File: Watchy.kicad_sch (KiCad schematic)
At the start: 74 parts, among them J1 FPC24(0.5MM), J2 USB_C_Receptacle_USB2.0, J4 Conn_01x01, J5 Conn_01x01, M1 Vibration_Motor, Q1 AO3400A, Q2 UMH3N, Q4 CJ2301, Q5 S8050, SW1 BTN, SW2 BTN, SW3 BTN, SW4 BTN, U1 ESP32-PICO-D4, U2 ME6211C33M5G-N, U3 CP2102, U4 BMA423, U5 TP4054, U6 PCF8563BS, Y1 32.768KHz

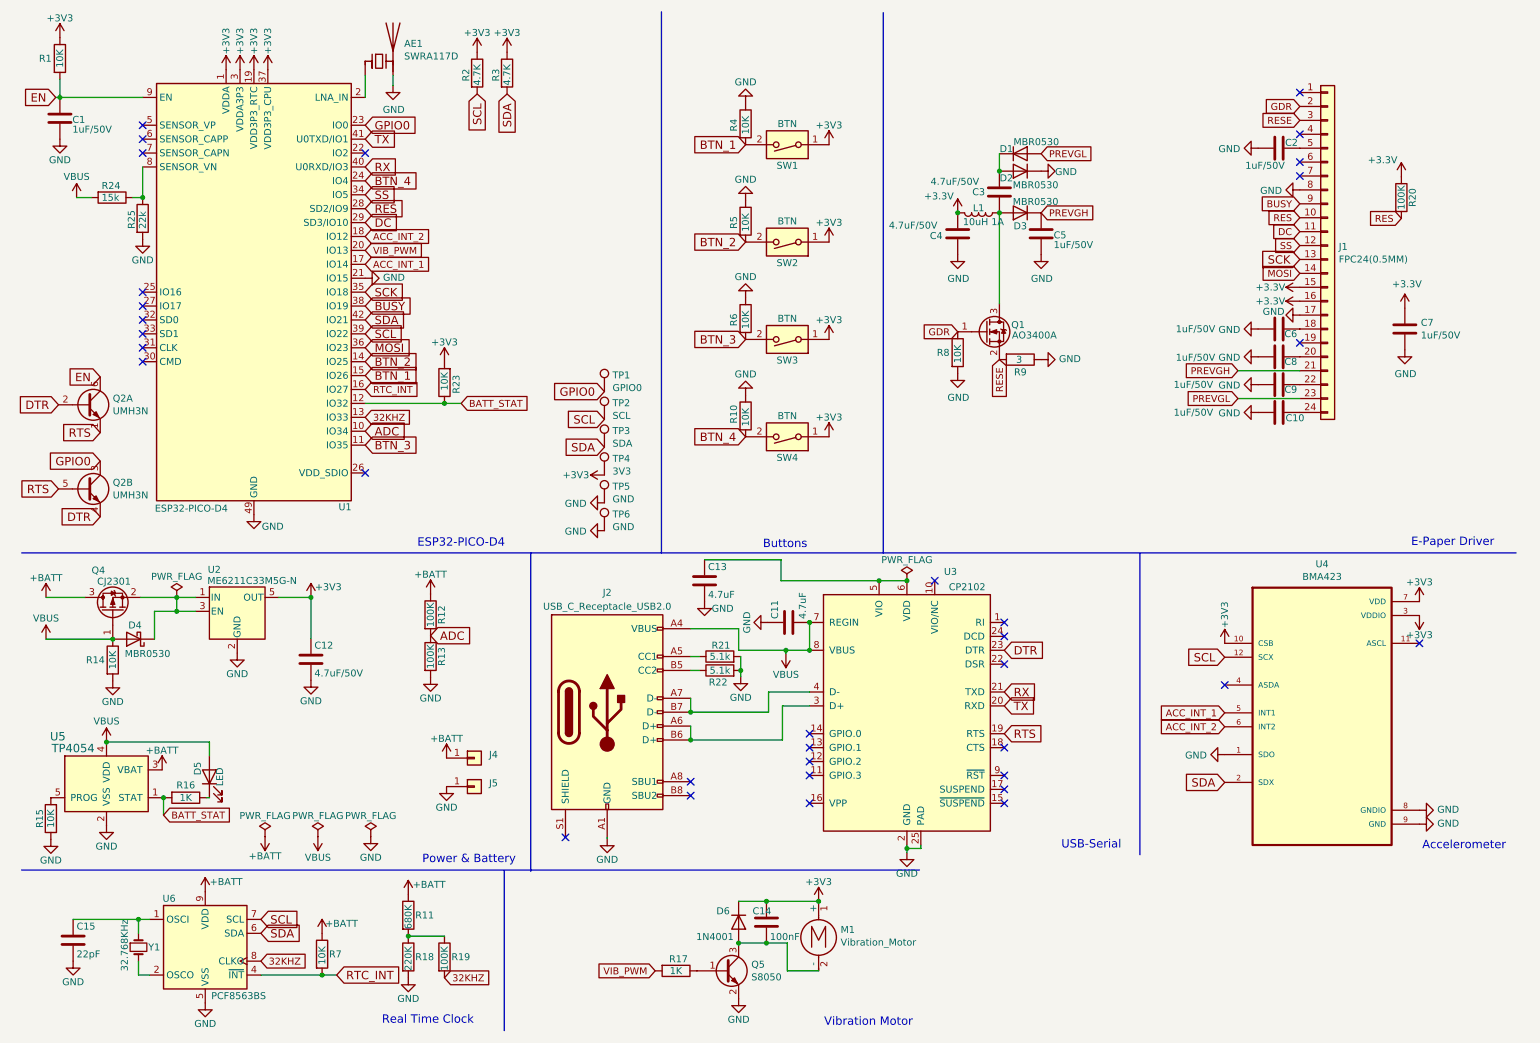
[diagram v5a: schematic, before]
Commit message: Rev2.0
New Rev with ESP32-S3 and PCF2131
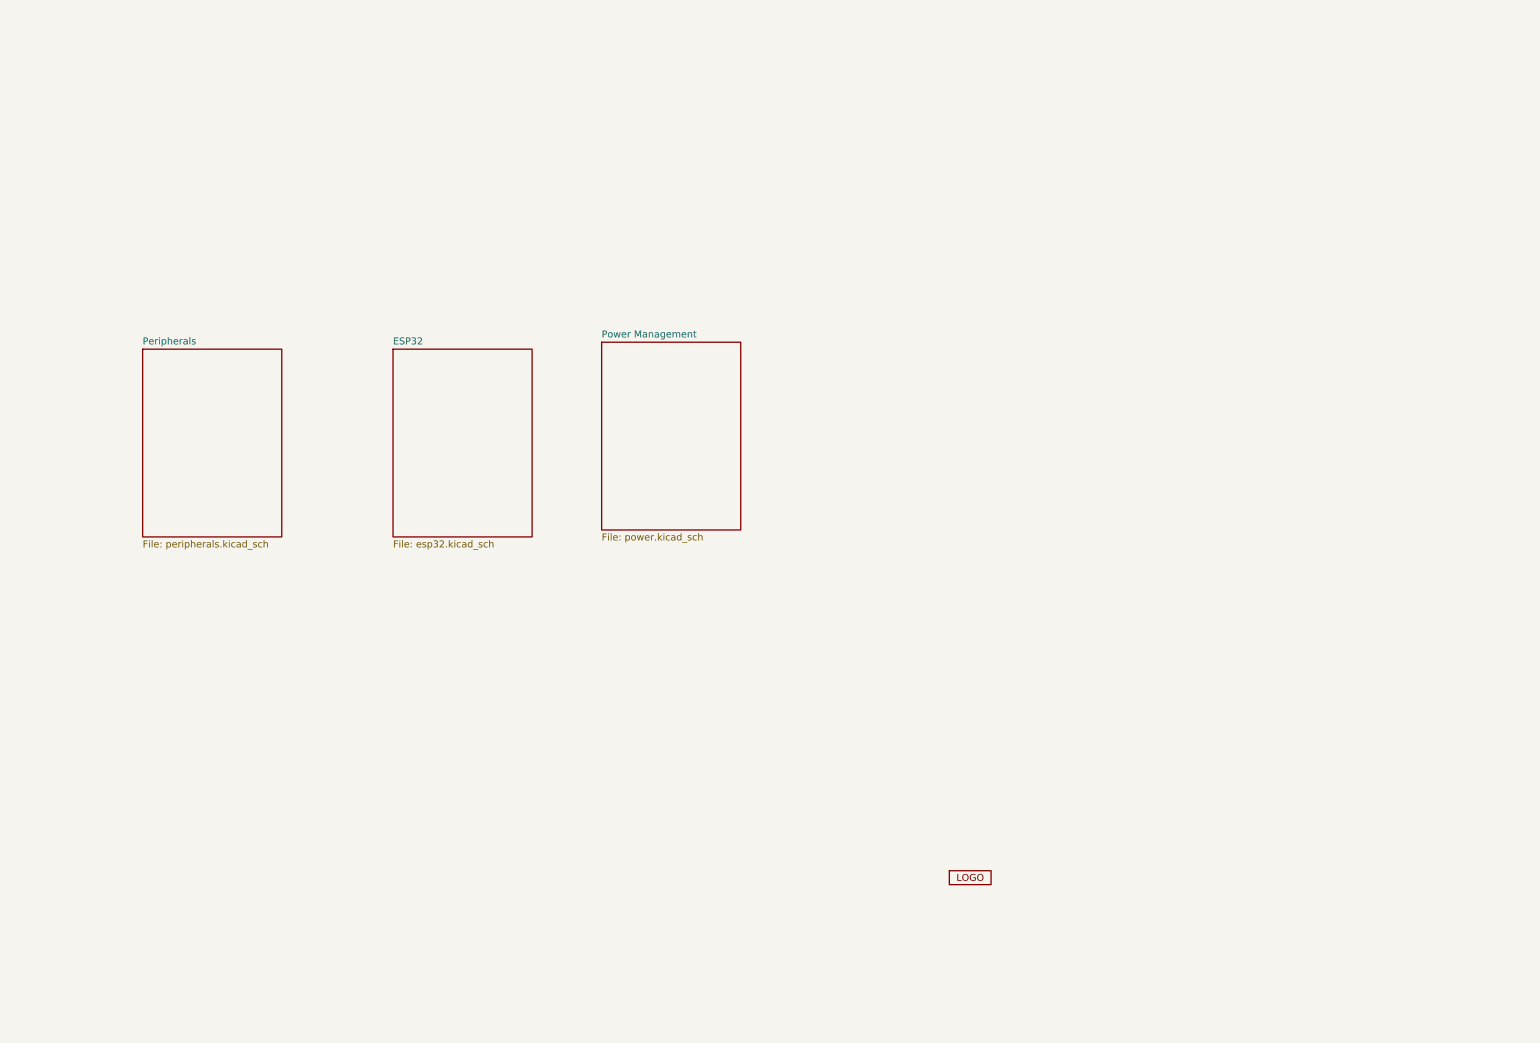
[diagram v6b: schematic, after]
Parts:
- removed AE1: SWRA117D, Watchy:SWRA117D, symbol Device:Antenna_Chip
- removed C1, C10, C2, C5, C6, C7, C8, C9: 1uF/50V, Capacitor_SMD:C_0603_1608Metric, symbol Device:C
- removed C11, C13: 4.7uF, Capacitor_SMD:C_0402_1005Metric, symbol Device:C
- removed C12, C3, C4: 4.7uF/50V, Watchy:C_0805, symbol Device:C
- removed C14: 100nF, Capacitor_SMD:C_0603_1608Metric, symbol Device:C
- removed C15: 22pF, Capacitor_SMD:C_0603_1608Metric, symbol Device:C
- removed D1, D2, D3: MBR0530, Watchy:D_SOD-123, symbol Device:D
- removed D4: MBR0530, Watchy:D_SOD-123, symbol Device:D_Schottky
- removed D5: LED, Watchy:LED_0603, symbol Device:LED
- removed D6: 1N4001, Watchy:D_SOD-123, symbol Diode:1N4001
- removed J1: FPC24(0.5MM), Watchy:24_Pins_0.5mm_Pitch_ZIF_Connector_UP, symbol Connector_Generic:Conn_01x24
- removed J2: USB_C_Receptacle_USB2.0, Connector_USB:USB_C_Receptacle_Palconn_UTC16-G, symbol Connector:USB_C_Receptacle_USB2.0
- removed J4, J5: Conn_01x01, Watchy:BatteryPads, symbol Connector_Generic:Conn_01x01
- removed L1: 10uH 1A, Inductor_SMD:L_Taiyo-Yuden_NR-40xx, symbol Device:L
- removed M1: Vibration_Motor, Watchy:Motor_Header, symbol Motor:Motor_DC
- removed Q1: AO3400A, Watchy:SOT-23, symbol Transistor_FET:DMN3042L
- removed Q2: UMH3N, Package_TO_SOT_SMD:SOT-363_SC-70-6, symbol Watchy-rescue:Q_DUAL_NPN_NPN_E1B1C2E2B2C1-Device
- removed Q4: CJ2301, Watchy:SOT-23, symbol Transistor_FET:BSS83P
- removed Q5: S8050, Watchy:SOT-23, symbol Device:Q_NPN_BEC
- removed R1, R10, R14, R15, R23, R4, R5, R6, R7, R8: 10K, Watchy:R_0402, symbol Device:R
- removed R11: 680K, Watchy:R_0402, symbol Device:R
- removed R12, R13, R19, R20: 100K, Watchy:R_0402, symbol Device:R
- removed R16, R17: 1K, Watchy:R_0402, symbol Device:R
- removed R18: 220K, Watchy:R_0402, symbol Device:R
- removed R2, R3: 4.7K, Watchy:R_0402, symbol Device:R
- removed R21, R22: 5.1k, Watchy:R_0402, symbol Device:R
- removed R24: 15k, Watchy:R_0402, symbol Device:R
- removed R25: 22k, Watchy:R_0402, symbol Device:R
- removed R9: 3, Watchy:R_0402, symbol Device:R
- removed SW1, SW2, SW3, SW4: BTN, Watchy:K2-1114SA-A4SW-06, symbol Switch:SW_DIP_x01
- removed TP1: GPIO0, TestPoint:TestPoint_Pad_D1.0mm, symbol Connector:TestPoint
- removed TP2: SCL, TestPoint:TestPoint_Pad_D1.0mm, symbol Connector:TestPoint
- removed TP3: SDA, TestPoint:TestPoint_Pad_D1.0mm, symbol Connector:TestPoint
- removed TP4: 3V3, TestPoint:TestPoint_Pad_D1.0mm, symbol Connector:TestPoint
- removed TP5, TP6: GND, TestPoint:TestPoint_Pad_D1.0mm, symbol Connector:TestPoint
- removed U1: ESP32-PICO-D4, Package_DFN_QFN:QFN-48-1EP_7x7mm_P0.5mm_EP5.15x5.15mm, symbol RF_Module:ESP32-PICO-D4
- removed U2: ME6211C33M5G-N, Watchy:SOT-23-5, symbol Regulator_Linear:TLV70033_SOT23-5
- removed U3: CP2102, Package_DFN_QFN:QFN-24-1EP_4x4mm_P0.5mm_EP2.6x2.6mm, symbol Watchy-rescue:CP2104-Interface_USB
- removed U4: BMA423, Package_LGA:LGA-12_2x2mm_P0.5mm, symbol Watchy:BMA423
- removed U5: TP4054, Package_TO_SOT_SMD:SOT-23-5, symbol Watchy-rescue:MCP73831-2-OT-Battery_Management
- removed U6: PCF8563BS, Package_DFN_QFN:DFN-10-1EP_3x3mm_P0.5mm_EP1.7x2.5mm, symbol Watchy:PCF8563BS
- removed Y1: 32.768KHz, Crystal:Crystal_SMD_3215-2Pin_3.2x1.5mm, symbol Device:Crystal_Small
- added A1: ~, Watchy:logoLM, symbol Watchy:LOGO
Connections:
- no-connect marks 34 -> 0
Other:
- added sheet ESP32 (esp32.kicad_sch)
- added sheet Peripherals (peripherals.kicad_sch)
- added sheet Power Management (power.kicad_sch)
- note removed: "Accelerometer"
- note removed: "Buttons"
- note removed: "E-Paper Driver"
- note removed: "ESP32-PICO-D4"
- note removed: "Power & Battery"
- note removed: "Real Time Clock"
- note removed: "USB-Serial"
- note removed: "Vibration Motor"
